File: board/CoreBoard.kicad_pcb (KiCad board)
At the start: 2 copper layers, 0 parts

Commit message: Layout edits
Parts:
- added C1: 10µF, Capacitor_SMD:C_1206_3216Metric_Pad1.33x1.80mm_HandSolder, F.Cu at (76.8, 121.3)
- added C2: 10µF, Capacitor_SMD:C_0603_1608Metric_Pad1.08x0.95mm_HandSolder, F.Cu at (76.8, 127.6)
- added C3: 0.1µF, Capacitor_SMD:C_0603_1608Metric_Pad1.08x0.95mm_HandSolder, F.Cu at (193.7, 110.3)
- added Conn10: Molex_SL_03, MRDT_Connectors:MOLEX_SL_03_Vertical, F.Cu at (160.0, 131.4)
- added Conn2: Molex_SL_04, MRDT_Connectors:MOLEX_SL_04_Vertical, F.Cu at (148.6, 131.4)
- added Conn3: Molex_SL_09, MRDT_Connectors:MOLEX_SL_09_Horizontal, F.Cu at (86.4, 81.9)
- added Conn4: Molex_SL_09, MRDT_Connectors:MOLEX_SL_09_Horizontal, F.Cu at (182.2, 62.2)
- added Conn5: Molex_SL_04, MRDT_Connectors:MOLEX_SL_04_Vertical, F.Cu at (97.6, 54.0)
- added Conn6: Molex_SL_04, MRDT_Connectors:MOLEX_SL_04_Vertical, F.Cu at (111.6, 54.0)
- added Conn7: Molex_SL_04, MRDT_Connectors:MOLEX_SL_04_Vertical, F.Cu at (125.6, 54.0)
- added Conn8: Molex_SL_04, MRDT_Connectors:MOLEX_SL_04_Vertical, F.Cu at (83.8, 54.0)
- added Conn9: Molex_SL_04, MRDT_Connectors:MOLEX_SL_04_Vertical, F.Cu at (134.0, 131.3)
- added D1: Green, LED_SMD:LED_0603_1608Metric_Pad1.05x0.95mm_HandSolder, F.Cu at (106.8, 128.6)
- added D10: Orange, LED_SMD:LED_0603_1608Metric_Pad1.05x0.95mm_HandSolder, F.Cu at (140.0, 113.4)
- added D11: Orange, LED_SMD:LED_0603_1608Metric_Pad1.05x0.95mm_HandSolder, F.Cu at (137.2, 99.1)
- added D12: Blue, LED_SMD:LED_0603_1608Metric_Pad1.05x0.95mm_HandSolder, F.Cu at (139.0, 80.4)
- added D13: Blue, LED_SMD:LED_0603_1608Metric_Pad1.05x0.95mm_HandSolder, F.Cu at (136.4, 80.4)
- added D14: Blue, LED_SMD:LED_0603_1608Metric_Pad1.05x0.95mm_HandSolder, F.Cu at (149.3, 84.8)
- added D15: Blue, LED_SMD:LED_0603_1608Metric_Pad1.05x0.95mm_HandSolder, F.Cu at (146.7, 84.8)
- added D16: Blue, LED_SMD:LED_0603_1608Metric_Pad1.05x0.95mm_HandSolder, F.Cu at (144.1, 84.8)
- added D17: Blue, LED_SMD:LED_0603_1608Metric_Pad1.05x0.95mm_HandSolder, F.Cu at (141.6, 84.8)
- added D18: Blue, LED_SMD:LED_0603_1608Metric_Pad1.05x0.95mm_HandSolder, F.Cu at (143.7, 62.8)
- added D19: Green, LED_SMD:LED_0603_1608Metric_Pad1.05x0.95mm_HandSolder, F.Cu at (114.6, 128.6)
- added D2: Green, LED_SMD:LED_0603_1608Metric_Pad1.05x0.95mm_HandSolder, F.Cu at (109.4, 128.6)
- added D20: MMSZ5240BT1G, MRDT_Devices:SOD-123_ONS-L, F.Cu at (90.8, 115.6)
- added D3: Green, LED_SMD:LED_0603_1608Metric_Pad1.05x0.95mm_HandSolder, F.Cu at (112.0, 128.6)
- added D4: Blue, LED_SMD:LED_0603_1608Metric_Pad1.05x0.95mm_HandSolder, F.Cu at (149.3, 80.4)
- added D5: Blue, LED_SMD:LED_0603_1608Metric_Pad1.05x0.95mm_HandSolder, F.Cu at (146.7, 80.4)
- added D6: Blue, LED_SMD:LED_0603_1608Metric_Pad1.05x0.95mm_HandSolder, F.Cu at (144.1, 80.4)
- added D7: Orange, LED_SMD:LED_0603_1608Metric_Pad1.05x0.95mm_HandSolder, F.Cu at (126.5, 124.4)
- added D8: Blue, LED_SMD:LED_0603_1608Metric_Pad1.05x0.95mm_HandSolder, F.Cu at (141.6, 80.4)
- added D9: Orange, LED_SMD:LED_0603_1608Metric_Pad1.05x0.95mm_HandSolder, F.Cu at (114.7, 115.1)
- added H1: MountingHole, MRDT_Drill_Holes:4_40_Hole, F.Cu at (167.6, 53.3)
- added H2: MountingHole, MRDT_Drill_Holes:4_40_Hole, F.Cu at (74.3, 54.0)
- added H3: MountingHole, MRDT_Drill_Holes:4_40_Hole, F.Cu at (74.3, 134.0)
- added H4: MountingHole, MRDT_Drill_Holes:4_40_Hole, F.Cu at (168.3, 134.0)
- added J1: RJ45_LED_Shielded, MRDT_Connectors:RJ45_Teensy, F.Cu at (186.2, 136.8)
- added J2: 768250002, CoreBoard:CONN_SD-76825-0100_02_MOL, F.Cu at (84.4, 126.2)
- added MOSFET1: TPC8132_LQS, MRDT_Devices:SOP-8_TOS-L, F.Cu at (97.8, 114.9)
- added Q1: AO3401A, CoreBoard:SOT-23-3L_AOS-L, F.Cu at (148.3, 62.4)
- added Q10: AO3401A, CoreBoard:SOT-23-3L_AOS-L, F.Cu at (137.5, 66.9)
- added Q11: AO3401A, CoreBoard:SOT-23-3L_AOS-L, F.Cu at (148.1, 62.8)
- added Q2: AO3401A, CoreBoard:SOT-23-3L_AOS-L, F.Cu at (148.3, 66.9)
- added Q3: AO3401A, CoreBoard:SOT-23-3L_AOS-L, F.Cu at (148.3, 71.4)
- added Q4: AO3401A, CoreBoard:SOT-23-3L_AOS-L, F.Cu at (148.3, 75.9)
- added Q5: AO3401A, CoreBoard:SOT-23-3L_AOS-L, F.Cu at (142.9, 62.4)
- added Q6: AO3401A, CoreBoard:SOT-23-3L_AOS-L, F.Cu at (142.9, 66.9)
- added Q7: AO3401A, CoreBoard:SOT-23-3L_AOS-L, F.Cu at (142.9, 71.4)
- added Q8: AO3401A, CoreBoard:SOT-23-3L_AOS-L, F.Cu at (142.9, 75.9)
- added Q9: AO3401A, CoreBoard:SOT-23-3L_AOS-L, F.Cu at (137.5, 62.4)
- added R1: 820, Resistor_SMD:R_0603_1608Metric_Pad0.98x0.95mm_HandSolder, F.Cu at (109.3, 133.0)
- added R10: 1k, Resistor_SMD:R_0603_1608Metric_Pad0.98x0.95mm_HandSolder, F.Cu at (93.3, 115.6)
- added R11: 1k, Resistor_SMD:R_0603_1608Metric_Pad0.98x0.95mm_HandSolder, F.Cu at (130.8, 124.4)
- added R12: 100, Resistor_SMD:R_0603_1608Metric_Pad0.98x0.95mm_HandSolder, F.Cu at (133.2, 66.7)
- added R13: 100, Resistor_SMD:R_0603_1608Metric_Pad0.98x0.95mm_HandSolder, F.Cu at (130.7, 66.7)
- added R15: 1k, Resistor_SMD:R_0603_1608Metric_Pad0.98x0.95mm_HandSolder, F.Cu at (119.0, 115.0)
- added R18: 1k, Resistor_SMD:R_0603_1608Metric_Pad0.98x0.95mm_HandSolder, F.Cu at (137.1, 95.6)
- added R2: 6.8k, Resistor_SMD:R_0603_1608Metric_Pad0.98x0.95mm_HandSolder, F.Cu at (111.8, 133.0)
- added R20: 100, Resistor_SMD:R_0603_1608Metric_Pad0.98x0.95mm_HandSolder, F.Cu at (128.2, 66.7)
- added R21: 100, Resistor_SMD:R_0603_1608Metric_Pad0.98x0.95mm_HandSolder, F.Cu at (125.7, 66.7)
- added R22: 100, Resistor_SMD:R_0603_1608Metric_Pad0.98x0.95mm_HandSolder, F.Cu at (149.2, 67.2)
- added R23: 3k, Resistor_SMD:R_0603_1608Metric_Pad0.98x0.95mm_HandSolder, F.Cu at (116.8, 133.0)
- added R24: 10k, Resistor_SMD:R_0603_1608Metric_Pad0.98x0.95mm_HandSolder, F.Cu at (140.8, 55.1)
- added R25: 10k, Resistor_SMD:R_0603_1608Metric_Pad0.98x0.95mm_HandSolder, F.Cu at (143.3, 55.1)
- added R26: 6.8k, Resistor_SMD:R_0603_1608Metric_Pad0.98x0.95mm_HandSolder, F.Cu at (145.8, 55.1)
- added R27: 6.8k, Resistor_SMD:R_0603_1608Metric_Pad0.98x0.95mm_HandSolder, F.Cu at (148.4, 55.1)
- added R28: 10k, Resistor_SMD:R_0603_1608Metric_Pad0.98x0.95mm_HandSolder, F.Cu at (150.9, 55.1)
- added R29: 10k, Resistor_SMD:R_0603_1608Metric_Pad0.98x0.95mm_HandSolder, F.Cu at (153.4, 55.1)
- added R3: 330, Resistor_SMD:R_0603_1608Metric_Pad0.98x0.95mm_HandSolder, F.Cu at (114.3, 133.0)
- added R30: 1k, Resistor_SMD:R_0603_1608Metric_Pad0.98x0.95mm_HandSolder, F.Cu at (144.3, 113.4)
- added R4: 100, Resistor_SMD:R_0603_1608Metric_Pad0.98x0.95mm_HandSolder, F.Cu at (133.2, 62.3)
- added R5: 100, Resistor_SMD:R_0603_1608Metric_Pad0.98x0.95mm_HandSolder, F.Cu at (130.7, 62.3)
- added R6: 100, Resistor_SMD:R_0603_1608Metric_Pad0.98x0.95mm_HandSolder, F.Cu at (128.2, 62.3)
- added R7: 100, Resistor_SMD:R_0603_1608Metric_Pad0.98x0.95mm_HandSolder, F.Cu at (125.7, 62.3)
- added R8: 100, Resistor_SMD:R_0603_1608Metric_Pad0.98x0.95mm_HandSolder, F.Cu at (123.1, 62.3)
- added R9: 100, Resistor_SMD:R_0603_1608Metric_Pad0.98x0.95mm_HandSolder, F.Cu at (132.1, 80.9)
- added S1: 94HBB08T, Temp_Sensor:DIPS762W56P254L991H597Q6N, F.Cu at (125.7, 106.0)
- added SW11: SW_Wuerth_450301014042, Button_Switch_THT:SW_Slide-03_Wuerth-WS-SLTV_10x2.5x6.4_P2.54mm, F.Cu at (105.4, 95.6)
- added SW12: SW_Wuerth_450301014042, Button_Switch_THT:SW_Slide-03_Wuerth-WS-SLTV_10x2.5x6.4_P2.54mm, F.Cu at (105.5, 107.2)
- added SW13: SW_Wuerth_450301014042, Button_Switch_THT:SW_Slide-03_Wuerth-WS-SLTV_10x2.5x6.4_P2.54mm, F.Cu at (105.4, 119.0)
- added SW14: SW_Wuerth_450301014042, Button_Switch_THT:SW_Slide-03_Wuerth-WS-SLTV_10x2.5x6.4_P2.54mm, F.Cu at (152.4, 96.6)
- added SW15: SW_Wuerth_450301014042, Button_Switch_THT:SW_Slide-03_Wuerth-WS-SLTV_10x2.5x6.4_P2.54mm, F.Cu at (152.4, 108.1)
- added SW16: SW_Wuerth_450301014042, Button_Switch_THT:SW_Slide-03_Wuerth-WS-SLTV_10x2.5x6.4_P2.54mm, F.Cu at (152.4, 119.6)
- added SW4: SW_Push, Button_Switch_SMD:SW_SPST_TL3305A, F.Cu at (129.4, 120.1)
- added SW6: SW_Push, Button_Switch_SMD:SW_SPST_TL3305A, F.Cu at (116.5, 109.1)
- added SW7: SW_Push, Button_Switch_SMD:SW_SPST_TL3305A, F.Cu at (142.9, 109.1)
- added SW8: SW_Push, Button_Switch_SMD:SW_SPST_TL3305A, F.Cu at (129.5, 97.8)
- added U1: 74VHC138FT, CoreBoard:TSSOP16B_TOS-L, F.Cu at (131.2, 73.0)
- added U2: OKI-78SR-12_1.0-W36H-C, Converter_DCDC:Converter_DCDC_Murata_OKI-78SR_Horizontal, F.Cu at (92.7, 119.4)
- added U3: SHHD003A0A, MRDT_Devices:SHHD003A0A-SRZ_Surface_Mount, F.Cu at (73.1, 110.5)
- added U4: GY-521, CoreBoard:GY-521, F.Cu at (190.8, 97.5)
- added U5: Teensy4.1_DEV-16771, MRDT_Shields:Teensy_4_1_Ethernet, F.Cu at (167.6, 94.0)
- added U6: MCP9808-E/MS, Temp_Sensor:MSOP8_MC_MCH-L, F.Cu at (159.4, 55.2)

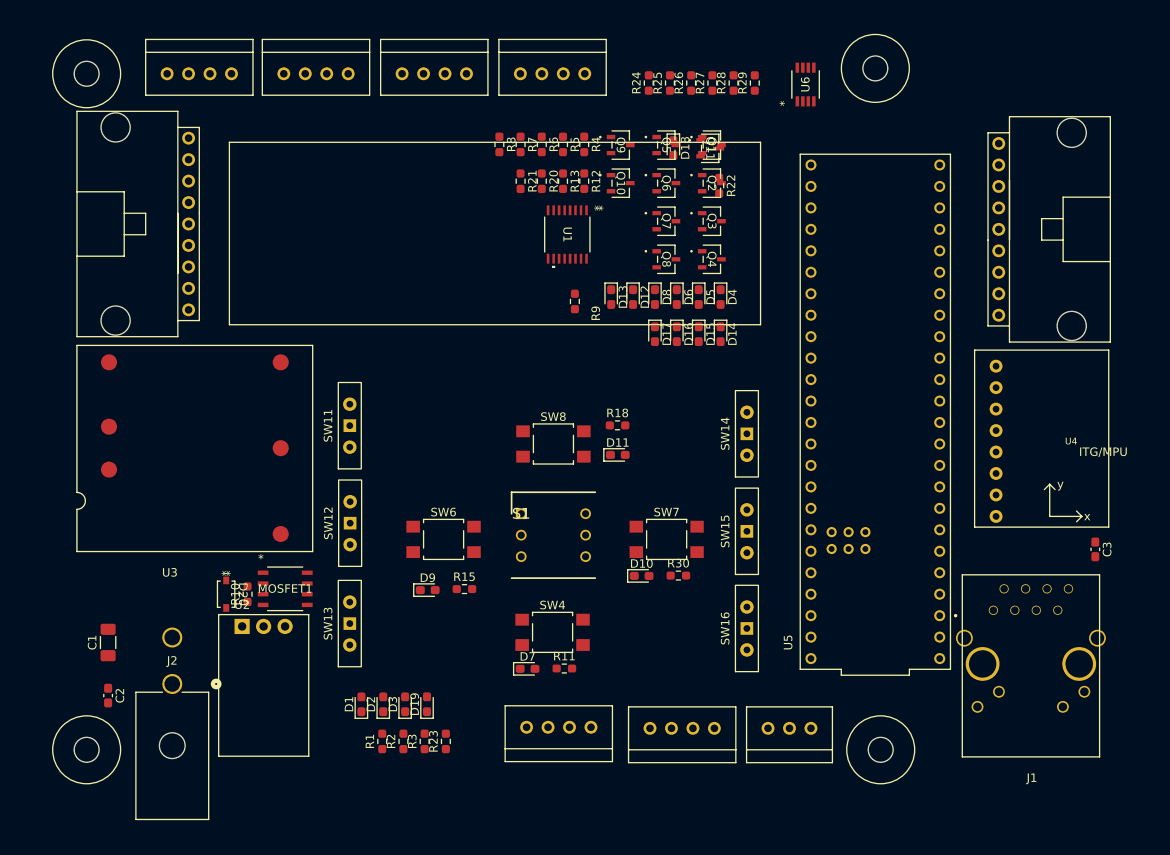
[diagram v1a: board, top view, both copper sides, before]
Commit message: routed core board
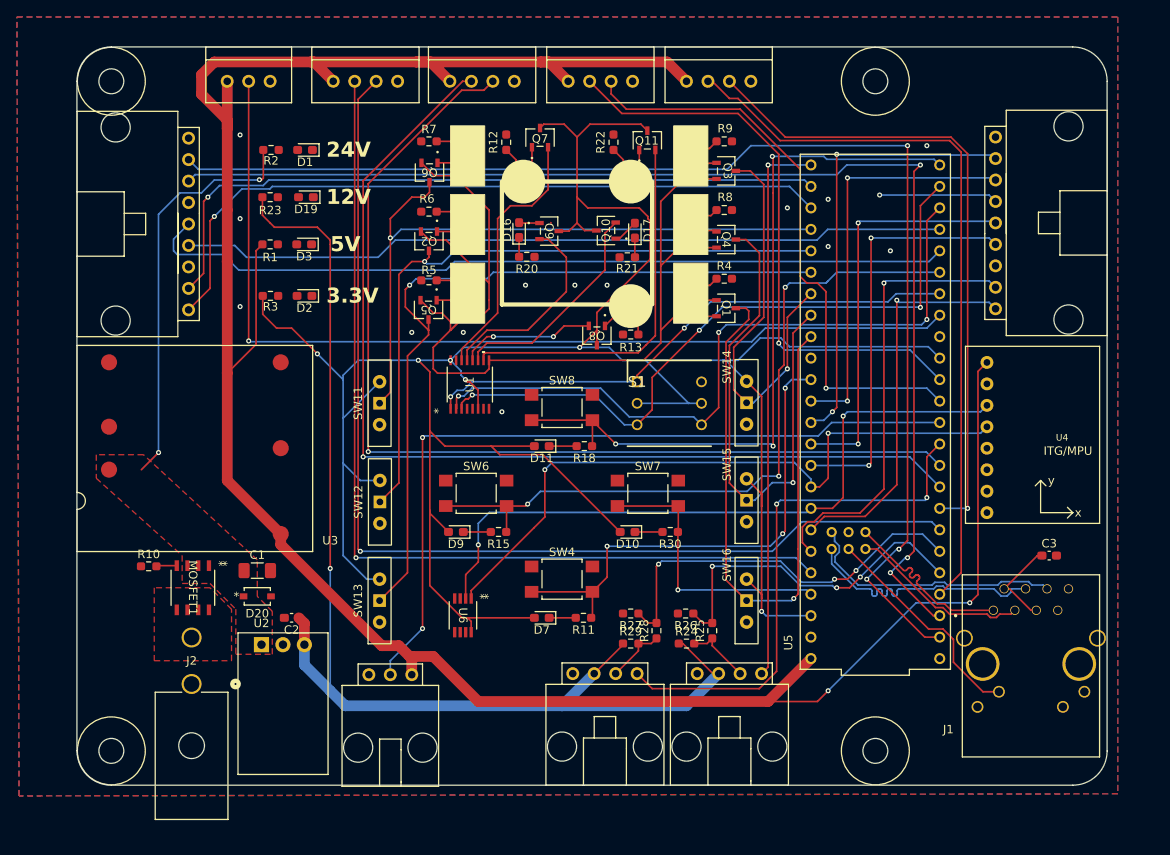
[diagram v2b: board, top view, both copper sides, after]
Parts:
- added Conn1: Molex_SL_03, MRDT_Connectors:MOLEX_SL_03_Vertical, F.Cu at (90.9, 54.9)
- Conn10: footprint MRDT_Connectors:MOLEX_SL_03_Vertical -> MRDT_Connectors:MOLEX_SL_03_Horizontal
- Conn2, Conn9: footprint MRDT_Connectors:MOLEX_SL_04_Vertical -> MRDT_Connectors:MOLEX_SL_04_Horizontal
- moved U6 74.8 mm to (118.8, 118.1), turned to -90 degrees
- moved R2 71.7 mm to (96.1, 63.0), turned to 0 degrees
- moved R29 67.9 mm to (138.7, 121.4), turned to 0 degrees
- moved R23 67.7 mm to (96.0, 68.6), turned to 0 degrees
- moved R24 66.5 mm to (145.3, 121.4), turned to 0 degrees
- moved D1 65.9 mm to (100.1, 63.0), turned to 180 degrees
- moved R28 65.5 mm to (141.7, 119.9)
- moved R25 65.0 mm to (148.3, 119.9)
- moved R27 63.5 mm to (138.7, 117.9), turned to 180 degrees
- moved R26 62.8 mm to (145.2, 117.9), turned to 180 degrees
- moved D19 61.7 mm to (100.2, 68.6), turned to 180 degrees
- moved R1 60.3 mm to (96.0, 74.2), turned to 0 degrees
- moved R3 55.8 mm to (96.0, 80.3), turned to 0 degrees
- moved D3 55.7 mm to (100.0, 74.2), turned to 180 degrees
- moved D2 49.2 mm to (100.1, 80.3), turned to 180 degrees
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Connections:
- Conn10 pad 2: /Lighting/NeoPixel -> /Lighting/Lighting_Panel
- D20 pad 1: +24V -> VCC
- MOSFET1 pad 1: +24V -> VCC
- MOSFET1 pad 2: +24V -> VCC
- MOSFET1 pad 3: +24V -> VCC
- Q11 pad 2: /Selection LEDs/Rightmast -> /Selection LEDs/RightMast
- U1 pad 10: /Selection LEDs/Spare2 -> /Selection LEDs/RightMast
- U1 pad 11: /Selection LEDs/Spare1 -> /Selection LEDs/Spare2
- U1 pad 13: /Selection LEDs/LeftMast -> /Selection LEDs/Spare1
- U1 pad 14: /Selection LEDs/Rightmast -> /Selection LEDs/LeftMast
- U1 pad 15: /Selection LEDs/Off -> unconnected-(U1-*Y0-Pad15)
- U5 pad 10: /Selection LEDs/BL_EN -> /Lighting/Lighting_Panel
- U5 pad 25: unconnected-(U5-A11-Pad25) -> /Lighting/RGB_Strip
- U5 pad 33: /Teensy/FPWM1 -> /Fans/PWM1
- U5 pad 36: /Selection LEDs/ML_EN -> /Selection LEDs/FL_EN
- U5 pad 37: /Selection LEDs/FL_EN -> /Selection LEDs/ML_EN
- U5 pad 38: /Lighting/NeoPixel -> /Selection LEDs/BL_EN
- U5 pad 39: /Selection LEDs/BR_EN -> /Selection LEDs/FR_EN
- U5 pad 41: /Selection LEDs/FR_EN -> /Selection LEDs/BR_EN
- U5 pad 9: /Teensy/FPWM2 -> /Fans/PWM2
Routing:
- net +3.3V: track 0.00 -> 336.5 mm, vias 0 -> 6
- net +5V: track 0.00 -> 286.5 mm, vias 0 -> 2
- net /Motor VESCs/FL_RX: track 0.00 -> 151.7 mm, vias 0 -> 3
- net /Motor VESCs/FL_TX: track 0.00 -> 145.2 mm, vias 0 -> 3
- net +12V: track 0.00 -> 139.7 mm, vias 0 -> 1
- net /Gimbal Servos/Spare2: track 0.00 -> 127.0 mm, vias 0 -> 1
- net /Gimbal Servos/LeftPan: track 0.00 -> 120.1 mm, vias 0 -> 1
- net /Gimbal Servos/LeftTilt: track 0.00 -> 119.8 mm, vias 0 -> 1
- net /Selection LEDs/Wheels: track 0.00 -> 119.2 mm
- net /Lighting/RGB_Strip: track 0.00 -> 113.9 mm, vias 0 -> 1
- net /Gimbal Servos/Spare1: track 0.00 -> 111.0 mm, vias 0 -> 1
- net /Motor VESCs/ML_RX: track 0.00 -> 96.5 mm
- net /Lighting/Lighting_Panel: track 0.00 -> 91.6 mm, vias 0 -> 2
- net /Motor VESCs/ML_TX: track 0.00 -> 90.8 mm
- net /Selection LEDs/BL_EN: track 0.00 -> 90.6 mm, vias 0 -> 1
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- added copper zone on B.Cu, net GND
- added copper zone on F.Cu, net GND
- added copper zone on F.Cu, net Net-(J2-Pad2)
- added copper zone on F.Cu, net VCC
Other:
- board outline added: 121.9 x 87.4 mm
- board text added: "12V"
- board text added: "24V"
- board text added: "3.3V"
- board text added: "5V"

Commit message: added 3d model for rotary encoder
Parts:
- S1: footprint Temp_Sensor:DIPS762W56P254L991H597Q6N -> CoreBoard:DIPS762W56P254L991H597Q6N
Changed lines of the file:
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@@
 		)
 	)
-	(footprint "Temp_Sensor:DIPS762W56P254L991H597Q6N"
+	(footprint "CoreBoard:DIPS762W56P254L991H597Q6N"
 		(layer "F.Cu")
 		(at 139.446 90.438)
@@
 		)
 		(embedded_fonts no)
-		(model "94HBB08T.stp"
+		(model "${KIPRJMOD}/../lib/Models/94HBB08T.stp"
 			(offset
 				(xyz 3.809999886 -2.539999924 6.340000057)

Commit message: route
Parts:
- moved U6 36.9 mm to (155.7, 117.9)
- moved U4 29.6 mm to (194.3, 126.2)
- moved C3 22.2 mm to (193.5, 89.4)
- moved J1 21.7 mm to (190.9, 115.6)
- moved R29 15.3 mm to (123.5, 123.4)
- moved R27 12.9 mm to (127.1, 123.4), turned to 0 degrees
- moved R28 11.6 mm to (130.7, 123.4), turned to 0 degrees
- moved R2 9.81 mm to (105.3, 66.5), turned to 180 degrees
- moved R23 9.46 mm to (105.3, 70.6), turned to 180 degrees
- moved R3 9.37 mm to (105.3, 78.7), turned to 180 degrees
- moved R1 9.26 mm to (105.3, 74.7), turned to 180 degrees
- moved Conn2 8.71 mm to (145.5, 126.1)
- moved Conn9 8.71 mm to (130.8, 126.1)
- moved Q8 7.67 mm to (127.1, 84.1)
- moved R13 7.54 mm to (131.2, 84.0)
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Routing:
- net +3.3V: track 336.5 -> 259.2 mm, vias 6 -> 4
- net /Fans/PWM2: track 63.0 -> 0.00 mm, vias 2 -> 0
- net VCC: track 48.6 -> 108.6 mm
- net /Teensy/Left: track 86.0 -> 118.1 mm, vias 3 -> 2
- net LED: track 26.4 -> 57.6 mm
- net /Motor VESCs/BR_TX: track 46.3 -> 73.5 mm, vias 1 -> 0
- net /Selection LEDs/FL_EN: track 79.7 -> 105.9 mm, vias 1 -> 3
- net /Fans/Tach2: track 47.3 -> 68.4 mm, vias 3 -> 0
- net /Selection LEDs/RTRY4: track 80.1 -> 101.2 mm, vias 3 -> 4
- net /Selection LEDs/RTRY1: track 64.8 -> 85.7 mm, vias 2 -> 3
- net /Selection LEDs/RTRY2: track 83.5 -> 104.2 mm, vias 3 -> 4
- net /Selection LEDs/ML_EN: track 79.5 -> 100.0 mm, vias 1 -> 3
- net /Motor VESCs/BR_RX: track 52.8 -> 71.2 mm, vias 1 -> 0
- net +5V: track 286.5 -> 304.7 mm, vias 2 -> 0
- net /Selection LEDs/Spare2: track 26.2 -> 41.0 mm, vias 0 -> 2
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- removed copper zone on F.Cu, net Net-(J2-Pad2)
- removed copper zone on F.Cu, net VCC
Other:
- board size 121.9 x 87.4 mm -> 127 x 88.9 mm

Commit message: Update CoreBoard.kicad_pcb
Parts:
- moved J1 29.7 mm to (176.4, 141.6)
- moved C3 29.7 mm to (179.0, 115.3)
- moved U4 28.2 mm to (189.7, 98.4)
- moved H1 22.4 mm to (190.5, 54.9)
- moved H4 22.4 mm to (190.5, 135.6)
- moved U6 17.2 mm to (157.7, 134.9), turned to 180 degrees
- moved U5 10.6 mm to (165.1, 83.1)
- moved Conn4 5.69 mm to (181.1, 62.5)
- moved Conn3 0.10 mm to (86.6, 82.8)
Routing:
- net /Fans/PWM2: track 0.00 -> 95.5 mm, vias 0 -> 2
- net +5V: track 304.7 -> 244.9 mm, vias 0 -> 2
- net +3.3V: track 259.2 -> 308.1 mm
- net /Teensy/Left: track 118.1 -> 86.1 mm, vias 2 -> 1
- net /Selection LEDs/FL_EN: track 105.9 -> 75.7 mm, vias 3 -> 1
- net /Accelerometer/AccSDA: track 65.0 -> 95.0 mm, vias 1 -> 0
- net /Gimbal Servos/LeftPan: track 114.7 -> 85.1 mm, vias 1 -> 2
- net /Gimbal Servos/LeftTilt: track 108.4 -> 80.3 mm, vias 1 -> 2
- net /Teensy/Back: track 65.6 -> 93.5 mm
- net /Lighting/Lighting_Panel: track 94.3 -> 119.9 mm
- net /Gimbal Servos/BackTilt: track 82.9 -> 59.4 mm, vias 1 -> 2
- net /Accelerometer/AccSCL: track 70.8 -> 92.4 mm, vias 1 -> 0
- net /Gimbal Servos/BackPan: track 81.1 -> 59.7 mm, vias 1 -> 2
- net /Motor VESCs/FL_TX: track 148.9 -> 169.8 mm
- net /Selection LEDs/BR_EN: track 74.7 -> 53.9 mm, vias 1 -> 3
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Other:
- board size 127 x 88.9 mm -> 121.4 x 88.9 mm

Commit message: route
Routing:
- net +5V: track 244.9 -> 290.3 mm, vias 2 -> 4
- net GND: track 0.00 -> 35.2 mm, vias 0 -> 11
- net +3.3V: track 308.1 -> 340.7 mm, vias 4 -> 7
- net /Teensy/Back: track 93.5 -> 83.4 mm
- net /Motor VESCs/ML_TX: vias 2 -> 1

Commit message: gnd
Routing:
- net +5V: track 290.3 -> 287.9 mm
- net /Selection LEDs/MR_EN: vias 1 -> 3
- net /Selection LEDs/RTRY1: vias 5 -> 7
- net GND: vias 11 -> 12
- net /Selection LEDs/Wheels: vias 2 -> 4

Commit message: pcb refine
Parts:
- added G***: LOGO, MRDT_Silkscreens:0_MRDT_Logo_10mm, F.Cu at (130.6, 103.9)
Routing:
- net Tx-: track 32.0 -> 28.9 mm
- net Tx+: track 32.0 -> 28.9 mm
- net LED: track 40.7 -> 38.7 mm, vias 3 -> 1
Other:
- board text added: "AIDAN CALLAWAY"
- board text added: "BENJAMIN MOGG"
